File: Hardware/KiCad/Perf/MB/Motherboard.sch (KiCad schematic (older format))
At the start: 59 parts, among them P1 Power input, U1 STM32F100ZE, U2 LM29237-3.3, Y1 24MHz

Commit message: sdfghjkl
sdfghjklø
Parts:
- added C18: 1µF, symbol CP1_Small
- added C19: 10nF, symbol CP1_Small
- R2, R3: renamed from R?; value R -> 4,7k
- gave numbers to parts that had none: 46
- renumbered C4 to C17
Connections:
- net +3V3: now also U1.32 (Vref+), U1.33 (Vdda), U1.6 (VBAT), C18.1, C19.1
- net GND: now also P2.9 (P9), U1.30 (Vssa), U1.31 (Vref-), C18.2, C19.2; no longer P2.1 (P1)
- net TIM 2 CH 1: now also P7.28 (P28); no longer U3.3 (A1)
- net TIM 2 CH 2: now also P7.30 (P30); no longer U3.4 (A2)
- net TIM 2 CH 3: now also P7.32 (P32); no longer U3.5 (A3)
- net TIM 2 CH 4: now also P7.34 (P34); no longer U3.6 (A4)
- net TIM 3 CH 1: now also U3.6 (A4); no longer P7.20 (P20), U3.7 (A5)
- net TIM 3 CH 2: now also U3.5 (A3); no longer P7.22 (P22), U3.8 (A6)
- net TIM 3 CH 3: now also U3.4 (A2); no longer P7.24 (P24), U3.9 (A7)
- net TIM 3 CH 4: now also U3.3 (A1); no longer P7.26 (P26), U3.10 (A8)
- net TIM 4 CH 1: now also U3.10 (A8); no longer P7.28 (P28)
- net TIM 4 CH 2: now also U3.9 (A7); no longer P7.30 (P30)
- net TIM 4 CH 3: now also U3.8 (A6); no longer P7.32 (P32)
- net TIM 4 CH 4: now also U3.7 (A5); no longer P7.34 (P34)
- net at U1.23 (OSC_IN): now also C1.1, Y1.1
- net at R1.1: now also U1.24 (OSC_OUT)
- net at P2.5 (P5), U3.18 (B4): now also R8.2; no longer R7.2
- new net: P2.1 (P1), R4.2, U3.14 (B8)
- new net: P2.2 (P2), R5.2, U3.15 (B7)
- new net: P2.3 (P3), R6.2, U3.16 (B6)
- new net: P2.4 (P4), R7.2, U3.17 (B5)
- new net: P2.6 (P6), R9.2, U3.19 (B3)
- new net: P2.7 (P7), R10.2, U3.20 (B2)
- new net: P2.8 (P8), R11.2, U3.21 (B1)
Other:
- moved on the sheet: C1, C2, R1, Y1

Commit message: laying out motherboard and backplane
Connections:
- net ADC 10: now also P6.21 (P21); no longer P7.31 (P31)
- net ADC 11: now also P6.23 (P23); no longer P7.33 (P33)
- net ADC 12: now also P6.25 (P25); no longer P7.35 (P35)
- net ADC 13: now also P6.27 (P27); no longer P7.37 (P37)
- net GPIO_0: now also P7.22 (P22); no longer P6.25 (P25)
- net GPIO_1: now also P7.24 (P24); no longer P6.27 (P27)
- net GPIO_10: now also P7.37 (P37); no longer P6.4 (P4)
- net GPIO_11: now also P6.3 (P3); no longer P6.6 (P6)
- net GPIO_12: now also P6.5 (P5); no longer P6.3 (P3)
- net GPIO_13: now also P6.7 (P7); no longer P6.5 (P5)
- net GPIO_14: now also P6.9 (P9); no longer P6.7 (P7)
- net GPIO_15: now also P6.11 (P11); no longer P6.9 (P9)
- net GPIO_16: now also P7.20 (P20); no longer P7.10 (P10)
- net GPIO_17: now also P7.18 (P18); no longer P7.12 (P12)
- net GPIO_18: now also P7.16 (P16); no longer P7.14 (P14)
- net GPIO_19: now also P7.14 (P14); no longer P7.16 (P16)
- net GPIO_2: now also P7.26 (P26); no longer P6.29 (P29)
- net GPIO_20: now also P7.12 (P12); no longer P7.18 (P18)
- net GPIO_21: now also P7.4 (P4); no longer P7.3 (P3)
- net GPIO_22: now also P7.6 (P6); no longer P7.5 (P5)
- net GPIO_23: now also P7.8 (P8); no longer P7.7 (P7)
- net GPIO_24: now also P7.10 (P10); no longer P7.9 (P9)
- net GPIO_25: now also P7.15 (P15); no longer P7.11 (P11)
- net GPIO_27: now also P7.11 (P11); no longer P7.15 (P15)
- net GPIO_28: now also P7.9 (P9); no longer P7.17 (P17)
- net GPIO_29: now also P7.7 (P7); no longer P7.19 (P19)
- net GPIO_3: now also P7.28 (P28); no longer P6.31 (P31)
- net GPIO_30: now also P7.5 (P5); no longer P7.21 (P21)
- net GPIO_31: now also P7.3 (P3); no longer P7.23 (P23)
- net GPIO_4: now also P7.30 (P30); no longer P6.33 (P33)
- net GPIO_5: now also P7.32 (P32); no longer P6.35 (P35)
- net GPIO_6: now also P7.34 (P34); no longer P6.37 (P37)
- net GPIO_7: now also P7.31 (P31); no longer P7.25 (P25)
- net GPIO_8: now also P7.33 (P33); no longer P7.27 (P27)
- net GPIO_9: now also P7.35 (P35); no longer P7.29 (P29)
- net I2C 2 SCL: now also P6.4 (P4); no longer P6.8 (P8)
- net I2C 2 SDA: now also P6.6 (P6); no longer P6.10 (P10)
- net TIM 2 CH 1: now also P6.20 (P20); no longer P7.28 (P28)
- net TIM 2 CH 2: now also P6.22 (P22); no longer P7.30 (P30)
- net TIM 2 CH 3: now also P6.24 (P24); no longer P7.32 (P32)
- net TIM 2 CH 4: now also P6.26 (P26); no longer P7.34 (P34)
- net UART 4 RX: now also P7.27 (P27); no longer P6.22 (P22)
- net UART 4 TX: now also P7.29 (P29); no longer P6.20 (P20)
- net UART 5 RX: now also P7.23 (P23); no longer P6.26 (P26)
- net UART 5 TX: now also P7.25 (P25); no longer P6.24 (P24)
- net USART 2 CK: now also P7.17 (P17); no longer P6.15 (P15)
- net USART 2 RX: now also P7.19 (P19); no longer P6.13 (P13)
- net USART 2 TX: now also P7.21 (P21); no longer P6.11 (P11)
- net USART 3 CK: now also P6.17 (P17); no longer P6.21 (P21)
- net USART 3 CTS: now also P6.19 (P19); no longer P6.23 (P23)
- net USART 3 RX: now also P6.15 (P15); no longer P6.19 (P19)
- net USART 3 TX: now also P6.13 (P13); no longer P6.17 (P17)
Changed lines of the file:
@@
 Text GLabel 10400 13700 0    47   Input ~ 0
 JTCK-SWCLK
-Text GLabel 21500 12500 2    47   Input ~ 0
+Text GLabel 19100 12100 2    47   Input ~ 0
 TIM 2 CH 4
-Text GLabel 21500 12200 2    47   Input ~ 0
+Text GLabel 19100 11800 2    47   Input ~ 0
 TIM 2 CH 1
-Text GLabel 21500 12300 2    47   Input ~ 0
+Text GLabel 19100 11900 2    47   Input ~ 0
 TIM 2 CH 2
-Text GLabel 21500 12400 2    47   Input ~ 0
+Text GLabel 19100 12000 2    47   Input ~ 0
 TIM 2 CH 3
 Text GLabel 16200 3700 0    47   Input ~ 0
@@
 Text GLabel 19100 7200 0    47   Input ~ 0
 TIM 17
-Text GLabel 19100 11200 2    47   Input ~ 0
+Text GLabel 19100 11000 2    47   Input ~ 0
 I2C 2 SCL
-Text GLabel 19100 11300 2    47   Input ~ 0
+Text GLabel 19100 11100 2    47   Input ~ 0
 I2C 2 SDA
 Text GLabel 19100 12400 2    47   Input ~ 0
@@
 Text GLabel 19100 12700 2    47   Input ~ 0
 TIM 15 CH 2
-Text GLabel 20400 12400 0    47   Input ~ 0
+Text GLabel 18000 11900 0    47   Input ~ 0
 ADC 10
-Text GLabel 20400 12500 0    47   Input ~ 0
+Text GLabel 18000 12000 0    47   Input ~ 0
 ADC 11
-Text GLabel 20400 12600 0    47   Input ~ 0
+Text GLabel 18000 12100 0    47   Input ~ 0
 ADC 12
-Text GLabel 20400 12700 0    47   Input ~ 0
+Text GLabel 18000 12200 0    47   Input ~ 0
 ADC 13
-Text GLabel 19100 11800 2    47   Input ~ 0
+Text GLabel 20400 12300 0    47   Input ~ 0
 UART 4 TX
-Text GLabel 19100 11900 2    47   Input ~ 0
+Text GLabel 20400 12200 0    47   Input ~ 0
 UART 4 RX
-Text GLabel 19100 12000 2    47   Input ~ 0
+Text GLabel 20400 12100 0    47   Input ~ 0
 UART 5 TX
-Text GLabel 19100 12100 2    47   Input ~ 0
+Text GLabel 20400 12000 0    47   Input ~ 0
 UART 5 RX
-Text GLabel 18000 11400 0    47   Input ~ 0
+Text GLabel 20400 11900 0    47   Input ~ 0
 USART 2 TX
+Text GLabel 20400 11800 0    47   Input ~ 0
+USART 2 RX
 Text GLabel 18000 11500 0    47   Input ~ 0
-USART 2 RX
+USART 3 TX
+Text GLabel 18000 11600 0    47   Input ~ 0
+USART 3 RX
+Text GLabel 20400 11700 0    47   Input ~ 0
+USART 2 CK
 Text GLabel 18000 11700 0    47   Input ~ 0
-USART 3 TX
+USART 3 CK
 Text GLabel 18000 11800 0    47   Input ~ 0
-USART 3 RX
-Text GLabel 18000 11600 0    47   Input ~ 0
-USART 2 CK
-Text GLabel 18000 11900 0    47   Input ~ 0
-USART 3 CK
-Text GLabel 18000 12000 0    47   Input ~ 0
 USART 3 CTS
 Text GLabel 19100 7300 0    47   Input ~ 0
@@
 	16600 4200 16800 4200
 Wire Wire Line
-	18000 4600 16600 4600
+	16600 4600 18000 4600
 Wire Wire Line
 	17300 4600 17300 4750
 Connection ~ 16600 4300
 Wire Wire Line
-	18000 3400 18000 4600
+	18000 4600 18000 3400
 Wire Wire Line
 	18000 4300 17800 4300
@@
 	2900 7600 3000 7600
 Wire Wire Line
-	3000 8000 3000 7600
-Wire Wire Line
-	2000 8000 3000 8000
+	3000 7600 3000 8000
+Wire Wire Line
+	3000 8000 2000 8000
 Wire Wire Line
 	2000 8000 2000 7800
@@
 Text GLabel 21500 12700 2    47   Input ~ 0
 I2C 2 SDA
-Text GLabel 18000 12200 0    47   Input ~ 0
+Text GLabel 21500 12000 2    47   Input ~ 0
 GPIO_1
-Text GLabel 18000 12300 0    47   Input ~ 0
+Text GLabel 21500 12100 2    47   Input ~ 0
 GPIO_2
-Text GLabel 18000 12400 0    47   Input ~ 0
+Text GLabel 21500 12200 2    47   Input ~ 0
 GPIO_3
-Text GLabel 18000 12500 0    47   Input ~ 0
+Text GLabel 21500 12300 2    47   Input ~ 0
 GPIO_4
-Text GLabel 18000 12600 0    47   Input ~ 0
+Text GLabel 21500 12400 2    47   Input ~ 0
 GPIO_5
-Text GLabel 18000 12700 0    47   Input ~ 0
+Text GLabel 21500 12500 2    47   Input ~ 0
 GPIO_6
-Text GLabel 20400 12100 0    47   Input ~ 0
+Text GLabel 20400 12400 0    47   Input ~ 0
 GPIO_7
-Text GLabel 20400 12200 0    47   Input ~ 0
+Text GLabel 20400 12500 0    47   Input ~ 0
 GPIO_8
-Text GLabel 20400 12300 0    47   Input ~ 0
+Text GLabel 20400 12600 0    47   Input ~ 0
 GPIO_9
-Text GLabel 19100 11000 2    47   Input ~ 0
+Text GLabel 20400 12700 0    47   Input ~ 0
 GPIO_10
-Text GLabel 19100 11100 2    47   Input ~ 0
+Text GLabel 18000 11000 0    47   Input ~ 0
 GPIO_11
-Text GLabel 18000 11000 0    47   Input ~ 0
+Text GLabel 18000 11100 0    47   Input ~ 0
 GPIO_12
-Text GLabel 18000 11100 0    47   Input ~ 0
+Text GLabel 18000 11200 0    47   Input ~ 0
 GPIO_13
-Text GLabel 18000 11200 0    47   Input ~ 0
+Text GLabel 18000 11300 0    47   Input ~ 0
 GPIO_14
-Text GLabel 18000 11300 0    47   Input ~ 0
+Text GLabel 18000 11400 0    47   Input ~ 0
 GPIO_15
-Text GLabel 18000 12100 0    47   Input ~ 0
+Text GLabel 21500 11900 2    47   Input ~ 0
 GPIO_0
+Text GLabel 21500 11700 2    47   Input ~ 0
+GPIO_17
+Text GLabel 21500 11600 2    47   Input ~ 0
+GPIO_18
+Text GLabel 21500 11500 2    47   Input ~ 0
+GPIO_19
 Text GLabel 21500 11400 2    47   Input ~ 0
-GPIO_17
-Text GLabel 21500 11500 2    47   Input ~ 0
-GPIO_18
-Text GLabel 21500 11600 2    47   Input ~ 0
-GPIO_19
-Text GLabel 21500 11700 2    47   Input ~ 0
 GPIO_20
-Text GLabel 20400 11000 0    47   Input ~ 0
+Text GLabel 21500 11000 2    47   Input ~ 0
 GPIO_21
-Text GLabel 20400 11100 0    47   Input ~ 0
+Text GLabel 21500 11100 2    47   Input ~ 0
 GPIO_22
-Text GLabel 20400 11200 0    47   Input ~ 0
+Text GLabel 21500 11200 2    47   Input ~ 0
 GPIO_23
-Text GLabel 20400 11300 0    47   Input ~ 0
+Text GLabel 21500 11300 2    47   Input ~ 0
 GPIO_24
-Text GLabel 20400 11400 0    47   Input ~ 0
+Text GLabel 20400 11600 0    47   Input ~ 0
 GPIO_25
 Text GLabel 20400 11500 0    47   Input ~ 0
 GPIO_26
-Text GLabel 20400 11600 0    47   Input ~ 0
+Text GLabel 20400 11400 0    47   Input ~ 0
 GPIO_27
-Text GLabel 20400 11700 0    47   Input ~ 0
+Text GLabel 20400 11300 0    47   Input ~ 0
 GPIO_28
-Text GLabel 20400 11800 0    47   Input ~ 0
+Text GLabel 20400 11200 0    47   Input ~ 0
 GPIO_29
-Text GLabel 20400 11900 0    47   Input ~ 0
+Text GLabel 20400 11100 0    47   Input ~ 0
 GPIO_30
-Text GLabel 20400 12000 0    47   Input ~ 0
+Text GLabel 20400 11000 0    47   Input ~ 0
 GPIO_31
-Text GLabel 21500 11300 2    47   Input ~ 0
+Text GLabel 21500 11800 2    47   Input ~ 0
 GPIO_16
 $Comp

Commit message: updated footprints and some layout
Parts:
- removed P2: CONN_01X09, symbol CONN_01X09
- removed P4: CONN_01X08, symbol CONN_01X08
- added P2: CONN_01X10, symbol CONN_01X10
- added P4: CONN_01X05, symbol CONN_01X05
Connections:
- net GND: now also P2.10 (P10), P4.5 (P5)
- net I2C 2 SCL: now also P6.8 (P8), P4.3 (P3); no longer P6.4 (P4)
- net I2C 2 SDA: now also P6.10 (P10), P4.4 (P4); no longer P6.6 (P6)
- net TIM 16: now also P4.1 (P1)
- net TIM 17: now also P4.2 (P2)
- net at R4.2, U3.14 (B8): now also P2.1 (P1)
- net at R5.2, U3.15 (B7): now also P2.2 (P2)
- net at R6.2, U3.16 (B6): now also P2.3 (P3)
- net at R7.2, U3.17 (B5): now also P2.4 (P4)
- net at R8.2, U3.18 (B4): now also P2.5 (P5)
- net at R9.2, U3.19 (B3): now also P2.6 (P6)
- net at R10.2, U3.20 (B2): now also P2.7 (P7)
- net at R11.2, U3.21 (B1): now also P2.8 (P8)
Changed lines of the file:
@@
-$EndComp
-$Comp
-L CONN_01X09 P2
-U 1 1 55578F1D
-P 20000 3800
-F 0 "P2" H 20000 4300 50  0000 C CNN
-F 1 "CONN_01X09" V 20100 3800 50  0000 C CNN
-F 2 "" H 20000 3800 60  0000 C CNN
-F 3 "" H 20000 3800 60  0000 C CNN
-	1    20000 3800
-	1    0    0    1
 $EndComp
 $Comp
@@
 Text GLabel 19100 7200 0    47   Input ~ 0
 TIM 17
-Text GLabel 19100 11000 2    47   Input ~ 0
+Text GLabel 19100 11200 2    47   Input ~ 0
 I2C 2 SCL
-Text GLabel 19100 11100 2    47   Input ~ 0
+Text GLabel 19100 11300 2    47   Input ~ 0
 I2C 2 SDA
 Text GLabel 19100 12400 2    47   Input ~ 0
@@
 Wire Wire Line
 	17800 3500 19800 3500
-Wire Wire Line
-	19800 3400 19600 3400
-Wire Wire Line
-	19600 3400 19600 3200
 Wire Wire Line
 	19600 3200 19300 3200
@@
 Wire Wire Line
 	21200 11900 21500 11900
-$Comp
-L CONN_01X08 P4
-U 1 1 555F62F3
-P 19800 7450
-F 0 "P4" H 19800 7900 50  0000 C CNN
-F 1 "CONN_01X08" V 19900 7450 50  0000 C CNN
-F 2 "" H 19800 7450 60  0000 C CNN
-F 3 "" H 19800 7450 60  0000 C CNN
-	1    19800 7450
-	1    0    0    -1
-$EndComp
 Wire Wire Line
 	19100 7100 19600 7100
@@
 L GND #PWR036
 U 1 1 555F7849
-P 19500 7900
-F 0 "#PWR036" H 19500 7650 50  0001 C CNN
-F 1 "GND" H 19500 7750 50  0000 C CNN
-F 2 "" H 19500 7900 60  0000 C CNN
-F 3 "" H 19500 7900 60  0000 C CNN
-	1    19500 7900
-	1    0    0    -1
-$EndComp
-Wire Wire Line
-	19600 7800 19500 7800
-Wire Wire Line
-	19500 7800 19500 7900
+P 19500 7600
+F 0 "#PWR036" H 19500 7350 50  0001 C CNN
+F 1 "GND" H 19500 7450 50  0000 C CNN
+F 2 "" H 19500 7600 60  0000 C CNN
+F 3 "" H 19500 7600 60  0000 C CNN
+	1    19500 7600
+	1    0    0    -1
+$EndComp
+Wire Wire Line
+	19600 7500 19500 7500
+Wire Wire Line
+	19500 7500 19500 7600
 Text GLabel 2600 12700 0    47   Input ~ 0
 INT_GPIO_1
@@
 	18600 4400 18600 4200
 Connection ~ 18600 4200
+$Comp
+L CONN_01X10 P2
+U 1 1 5565FADF
+P 20000 3750
+F 0 "P2" H 20000 4300 50  0000 C CNN
+F 1 "CONN_01X10" V 20100 3750 50  0000 C CNN
+F 2 "" H 20000 3750 60  0000 C CNN
+F 3 "" H 20000 3750 60  0000 C CNN
+	1    20000 3750
+	1    0    0    1
+$EndComp
+Wire Wire Line
+	19800 3300 19600 3300
+Wire Wire Line
+	19600 3300 19600 3200
+$Comp
+L CONN_01X05 P4
+U 1 1 5566EDB3
+P 19800 7300
+F 0 "P4" H 19800 7600 50  0000 C CNN
+F 1 "CONN_01X05" V 19900 7300 50  0000 C CNN
+F 2 "" H 19800 7300 60  0000 C CNN
+F 3 "" H 19800 7300 60  0000 C CNN
+	1    19800 7300
+	1    0    0    -1
+$EndComp
 $EndSCHEMATC

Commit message: Small change to USART 2 pin layout from MB to Backplane
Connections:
- net GPIO_25: now also P7.11 (P11); no longer P7.15 (P15)
- net GPIO_26: now also P7.9 (P9); no longer P7.13 (P13)
- net GPIO_27: now also P7.7 (P7); no longer P7.11 (P11)
- net GPIO_28: now also P7.5 (P5); no longer P7.9 (P9)
- net GPIO_29: now also P7.3 (P3); no longer P7.7 (P7)
- net GPIO_30: no longer P7.5 (P5)
- net GPIO_31: no longer P7.3 (P3)
- net USART 2 CK: now also P7.13 (P13); no longer P7.17 (P17)
- net USART 2 RX: now also P7.15 (P15); no longer P7.19 (P19)
- net USART 2 TX: now also P7.17 (P17); no longer P7.21 (P21)
- net USART 2 CTS: now reaches U1.117 (PD3)
- net USART 2 CTS: now also P7.21 (P21)
- net USART 2 RTS: now reaches U1.118 (PD4)
- net USART 2 RTS: now also P7.19 (P19)
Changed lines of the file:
@@
 Text GLabel 20400 12000 0    47   Input ~ 0
 UART 5 RX
-Text GLabel 20400 11900 0    47   Input ~ 0
+Text GLabel 20400 11700 0    47   Input ~ 0
 USART 2 TX
-Text GLabel 20400 11800 0    47   Input ~ 0
+Text GLabel 20400 11600 0    47   Input ~ 0
 USART 2 RX
 Text GLabel 18000 11500 0    47   Input ~ 0
@@
 Text GLabel 18000 11600 0    47   Input ~ 0
 USART 3 RX
-Text GLabel 20400 11700 0    47   Input ~ 0
+Text GLabel 20400 11500 0    47   Input ~ 0
 USART 2 CK
 Text GLabel 18000 11700 0    47   Input ~ 0
@@
 Text GLabel 21500 11300 2    47   Input ~ 0
 GPIO_24
-Text GLabel 20400 11600 0    47   Input ~ 0
+Text GLabel 20400 11400 0    47   Input ~ 0
 GPIO_25
-Text GLabel 20400 11500 0    47   Input ~ 0
+Text GLabel 20400 11300 0    47   Input ~ 0
 GPIO_26
-Text GLabel 20400 11400 0    47   Input ~ 0
+Text GLabel 20400 11200 0    47   Input ~ 0
 GPIO_27
-Text GLabel 20400 11300 0    47   Input ~ 0
+Text GLabel 20400 11100 0    47   Input ~ 0
 GPIO_28
-Text GLabel 20400 11200 0    47   Input ~ 0
+Text GLabel 20400 11000 0    47   Input ~ 0
 GPIO_29
-Text GLabel 20400 11100 0    47   Input ~ 0
-GPIO_30
-Text GLabel 20400 11000 0    47   Input ~ 0
-GPIO_31
 Text GLabel 21500 11800 2    47   Input ~ 0
 GPIO_16
@@
 	1    0    0    -1
 $EndComp
+Text GLabel 12200 9200 2    47   Input ~ 0
+USART 2 RTS
+Text GLabel 12200 9100 2    47   Input ~ 0
+USART 2 CTS
+Wire Wire Line
+	11800 9100 12200 9100
+Wire Wire Line
+	12200 9200 11800 9200
+Text GLabel 20400 11800 0    47   Input ~ 0
+USART 2 RTS
+Text GLabel 20400 11900 0    47   Input ~ 0
+USART 2 CTS
 $EndSCHEMATC

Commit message: fixed adressing error on PERF eeprom
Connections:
- net GND: now also U4.1 (A0), U4.2 (A1), U4.3 (A2)
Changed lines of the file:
@@
 EESchema Schematic File Version 2
+LIBS:Motherboard-rescue
 LIBS:power
 LIBS:device
@@
 	3000 8000 2000 8000
 Wire Wire Line
-	2000 8000 2000 7800
+	2000 8000 2000 7500
 Wire Wire Line
 	2000 7800 2100 7800
@@
 Text GLabel 20400 11900 0    47   Input ~ 0
 USART 2 CTS
+Wire Wire Line
+	2000 7500 2100 7500
+Connection ~ 2000 7800
+Wire Wire Line
+	2100 7600 2000 7600
+Connection ~ 2000 7600
+Wire Wire Line
+	2100 7700 2000 7700
+Connection ~ 2000 7700
 $EndSCHEMATC

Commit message: Stuff is working!
Fixed thruster scaling where dividing by zero, and rounding messed up
the calculation.
PWM scaling to fit servo output fixed and working.
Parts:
- R12, R13: value R -> 4,7K
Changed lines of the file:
@@
 P 13000 5950
 F 0 "R12" V 13080 5950 50  0000 C CNN
-F 1 "R" V 13000 5950 50  0000 C CNN
+F 1 "4,7K" V 13000 5950 50  0000 C CNN
 F 2 "" V 12930 5950 30  0000 C CNN
 F 3 "" H 13000 5950 30  0000 C CNN
@@
 P 13400 5950
 F 0 "R13" V 13480 5950 50  0000 C CNN
-F 1 "R" V 13400 5950 50  0000 C CNN
+F 1 "4,7K" V 13400 5950 50  0000 C CNN
 F 2 "" V 13330 5950 30  0000 C CNN
 F 3 "" H 13400 5950 30  0000 C CNN

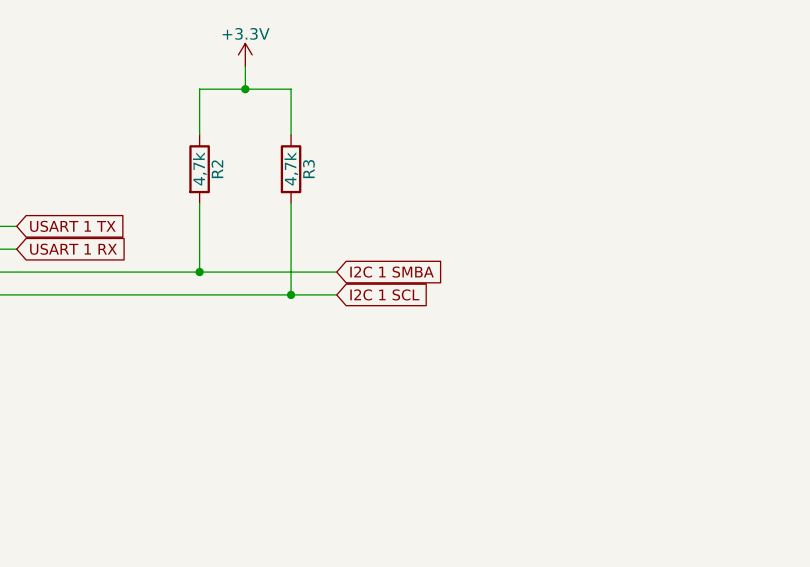
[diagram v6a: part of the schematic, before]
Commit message: Fixed i2c 1 layout error
Fixed wrong pin layout for i2c1
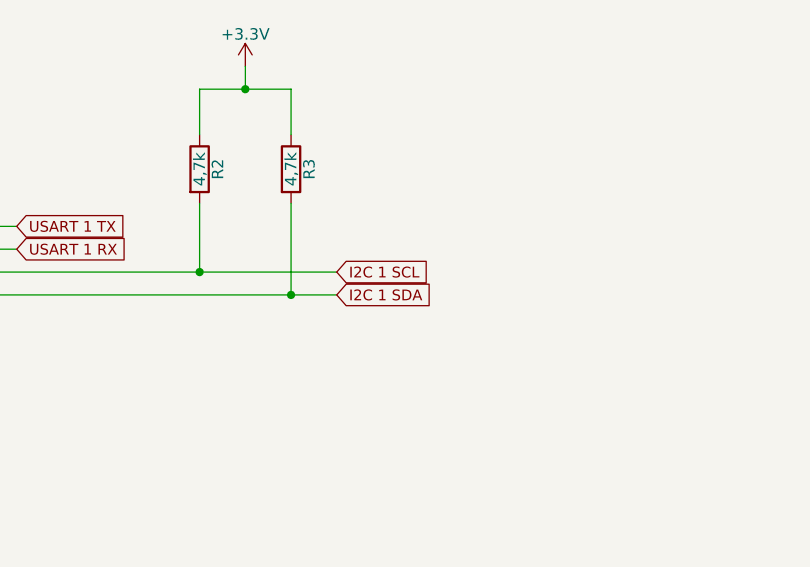
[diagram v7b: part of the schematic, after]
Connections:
- net I2C 1 SCL: now also P3.3 (P3), R2.2; no longer P3.4 (P4), R3.2
- net I2C 1 SDA: now also P3.4 (P4), R3.2
- net I2C 1 SMBA: no longer P3.3 (P3), R2.2
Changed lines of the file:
@@
 LIBS:memory
 LIBS:xilinx
-LIBS:special
 LIBS:microcontrollers
 LIBS:dsp
@@
 $EndComp
 Text GLabel 3500 4400 2    47   Input ~ 0
-I2C 1 SMBA
-Text GLabel 3500 4500 2    47   Input ~ 0
 I2C 1 SCL
 $Comp
@@
 	2100 7700 2000 7700
 Connection ~ 2000 7700
+Text GLabel 3500 4500 2    47   Input ~ 0
+I2C 1 SDA
 $EndSCHEMATC
